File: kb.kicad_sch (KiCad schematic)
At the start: 182 parts, among them J1 Conn_01x04_Female, J2 10029449-001RLF, SW1 RotaryEncoder_Switch, U1 Pico, U2 SN74AHCT125D

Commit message: fixing sk6812s
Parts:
- D101, D102, D103, D104, D105, D106, D107, D108, D109, D110, D111, D112, D113, D114, D115, D116, D117, D118, D119, D120, D121, D122, D123, D124, D125, D126, D127, D128, D129, D130, D131, D132, D133, D134, D135, D136, D137, D138, D139, D140, D141, D142, D143, D144: symbol LED:SK6812MINI -> LED:WS2812B
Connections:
- net +5V: now also D101.1 (VDD), D102.1 (VDD), D103.1 (VDD), D104.1 (VDD), D105.1 (VDD), D106.1 (VDD), D107.1 (VDD), D108.1 (VDD), D109.1 (VDD), D110.1 (VDD), D111.1 (VDD), D112.1 (VDD), D113.1 (VDD), D114.1 (VDD), D115.1 (VDD), D116.1 (VDD), D117.1 (VDD), D118.1 (VDD), D119.1 (VDD), D120.1 (VDD), D121.1 (VDD), D122.1 (VDD), D123.1 (VDD), D124.1 (VDD), D125.1 (VDD), D126.1 (VDD), D127.1 (VDD), D128.1 (VDD), D129.1 (VDD), D130.1 (VDD), D131.1 (VDD), D132.1 (VDD), D133.1 (VDD), D134.1 (VDD), D135.1 (VDD), D136.1 (VDD), D137.1 (VDD), D138.1 (VDD), D139.1 (VDD), D140.1 (VDD), D141.1 (VDD), D142.1 (VDD), D143.1 (VDD), D144.1 (VDD); no longer D101.4 (VDD), D102.4 (VDD), D103.4 (VDD), D104.4 (VDD), D105.4 (VDD), D106.4 (VDD), D107.4 (VDD), D108.4 (VDD), D109.4 (VDD), D110.4 (VDD), D111.4 (VDD), D112.4 (VDD), D113.4 (VDD), D114.4 (VDD), D115.4 (VDD), D116.4 (VDD), D117.4 (VDD), D118.4 (VDD), D119.4 (VDD), D120.4 (VDD), D121.4 (VDD), D122.4 (VDD), D123.4 (VDD), D124.4 (VDD), D125.4 (VDD), D126.4 (VDD), D127.4 (VDD), D128.4 (VDD), D129.4 (VDD), D130.4 (VDD), D131.4 (VDD), D132.4 (VDD), D133.4 (VDD), D134.4 (VDD), D135.4 (VDD), D136.4 (VDD), D137.4 (VDD), D138.4 (VDD), D139.4 (VDD), D140.4 (VDD), D141.4 (VDD), D142.4 (VDD), D143.4 (VDD), D144.4 (VDD)
- net COL0: now also J2.6
- net COL1: now also J2.7
- net COL2: now also J2.8
- net COL3: now also J2.9
- net COL4: now also J2.10
- net COL5: now also J2.11
- net COL6: now also J2.12
- net COL7: now also J2.13
- net COL8: now also J2.14
- net ENC_R1: now also J2.16, U1.10 (GPIO7); no longer J2.15, U1.11 (GPIO8)
- net ENC_R2: now also J2.15, U1.11 (GPIO8); no longer J2.16, U1.10 (GPIO7)
- net GND: now also D101.3 (VSS), D102.3 (VSS), D103.3 (VSS), D104.3 (VSS), D105.3 (VSS), D106.3 (VSS), D107.3 (VSS), D108.3 (VSS), D109.3 (VSS), D110.3 (VSS), D111.3 (VSS), D112.3 (VSS), D113.3 (VSS), D114.3 (VSS), D115.3 (VSS), D116.3 (VSS), D117.3 (VSS), D118.3 (VSS), D119.3 (VSS), D120.3 (VSS), D121.3 (VSS), D122.3 (VSS), D123.3 (VSS), D124.3 (VSS), D125.3 (VSS), D126.3 (VSS), D127.3 (VSS), D128.3 (VSS), D129.3 (VSS), D130.3 (VSS), D131.3 (VSS), D132.3 (VSS), D133.3 (VSS), D134.3 (VSS), D135.3 (VSS), D136.3 (VSS), D137.3 (VSS), D138.3 (VSS), D139.3 (VSS), D140.3 (VSS), D141.3 (VSS), D142.3 (VSS), D143.3 (VSS), D144.3 (VSS); no longer D101.2 (VSS), D102.2 (VSS), D103.2 (VSS), D104.2 (VSS), D105.2 (VSS), D106.2 (VSS), D107.2 (VSS), D108.2 (VSS), D109.2 (VSS), D110.2 (VSS), D111.2 (VSS), D112.2 (VSS), D113.2 (VSS), D114.2 (VSS), D115.2 (VSS), D116.2 (VSS), D117.2 (VSS), D118.2 (VSS), D119.2 (VSS), D120.2 (VSS), D121.2 (VSS), D122.2 (VSS), D123.2 (VSS), D124.2 (VSS), D125.2 (VSS), D126.2 (VSS), D127.2 (VSS), D128.2 (VSS), D129.2 (VSS), D130.2 (VSS), D131.2 (VSS), D132.2 (VSS), D133.2 (VSS), D134.2 (VSS), D135.2 (VSS), D136.2 (VSS), D137.2 (VSS), D138.2 (VSS), D139.2 (VSS), D140.2 (VSS), D141.2 (VSS), D142.2 (VSS), D143.2 (VSS), D144.2 (VSS)
- net RGB_5V: now also D101.4 (DIN); no longer D101.3 (DIN)
- net RGB_TO_RIGHT: now also D143.2 (DOUT); no longer D143.1 (DOUT)
- net ROW9: now reaches J2.1
- net ROW9: now also U1.21 (GPIO16)
- net ROW8: now reaches J2.2
- net ROW8: now also U1.22 (GPIO17)
- net ROW7: now reaches J2.3
- net ROW7: now also U1.24 (GPIO18)
- net ROW6: now reaches J2.4
- net ROW6: now also U1.25 (GPIO19)
- net ROW5: now reaches J2.5
- net ROW5: now also U1.26 (GPIO20)
- new net: D102.2 (DOUT), D103.4 (DIN)
- new net: D101.2 (DOUT), D102.4 (DIN)
- new net: D106.2 (DOUT), D107.4 (DIN)
- new net: D105.2 (DOUT), D106.4 (DIN)
- new net: D107.2 (DOUT), D108.4 (DIN)
- new net: D138.2 (DOUT), D139.4 (DIN)
- new net: D137.2 (DOUT), D138.4 (DIN)
- new net: D109.4 (DIN), D144.2 (DOUT)
- new net: D108.2 (DOUT), D144.4 (DIN)
- new net: D135.2 (DOUT), D136.4 (DIN)
- new net: D134.2 (DOUT), D135.4 (DIN)
- new net: D104.2 (DOUT), D105.4 (DIN)
- new net: D103.2 (DOUT), D104.4 (DIN)
- new net: D115.2 (DOUT), D116.4 (DIN)
- new net: D114.2 (DOUT), D115.4 (DIN)
- new net: D112.2 (DOUT), D113.4 (DIN)
- new net: D111.2 (DOUT), D112.4 (DIN)
- new net: D128.2 (DOUT), D129.4 (DIN)
- new net: D127.2 (DOUT), D128.4 (DIN)
- new net: D124.2 (DOUT), D125.4 (DIN)
- new net: D123.2 (DOUT), D124.4 (DIN)
- new net: D129.2 (DOUT), D130.4 (DIN)
- new net: D122.2 (DOUT), D123.4 (DIN)
- new net: D139.2 (DOUT), D140.4 (DIN)
- new net: D136.2 (DOUT), D137.4 (DIN)
- new net: D140.2 (DOUT), D141.4 (DIN)
- new net: D121.2 (DOUT), D122.4 (DIN)
- new net: D120.2 (DOUT), D121.4 (DIN)
- new net: D130.2 (DOUT), D131.4 (DIN)
- new net: D116.2 (DOUT), D117.4 (DIN)
- new net: D126.2 (DOUT), D127.4 (DIN)
- new net: D125.2 (DOUT), D126.4 (DIN)
- new net: D142.2 (DOUT), D143.4 (DIN)
- new net: D141.2 (DOUT), D142.4 (DIN)
- new net: D110.2 (DOUT), D111.4 (DIN)
- new net: D109.2 (DOUT), D110.4 (DIN)
- new net: D119.2 (DOUT), D120.4 (DIN)
- new net: D118.2 (DOUT), D119.4 (DIN)
- new net: D133.2 (DOUT), D134.4 (DIN)
- new net: D132.2 (DOUT), D133.4 (DIN)
- new net: D113.2 (DOUT), D114.4 (DIN)
- new net: D131.2 (DOUT), D132.4 (DIN)
- new net: D117.2 (DOUT), D118.4 (DIN)

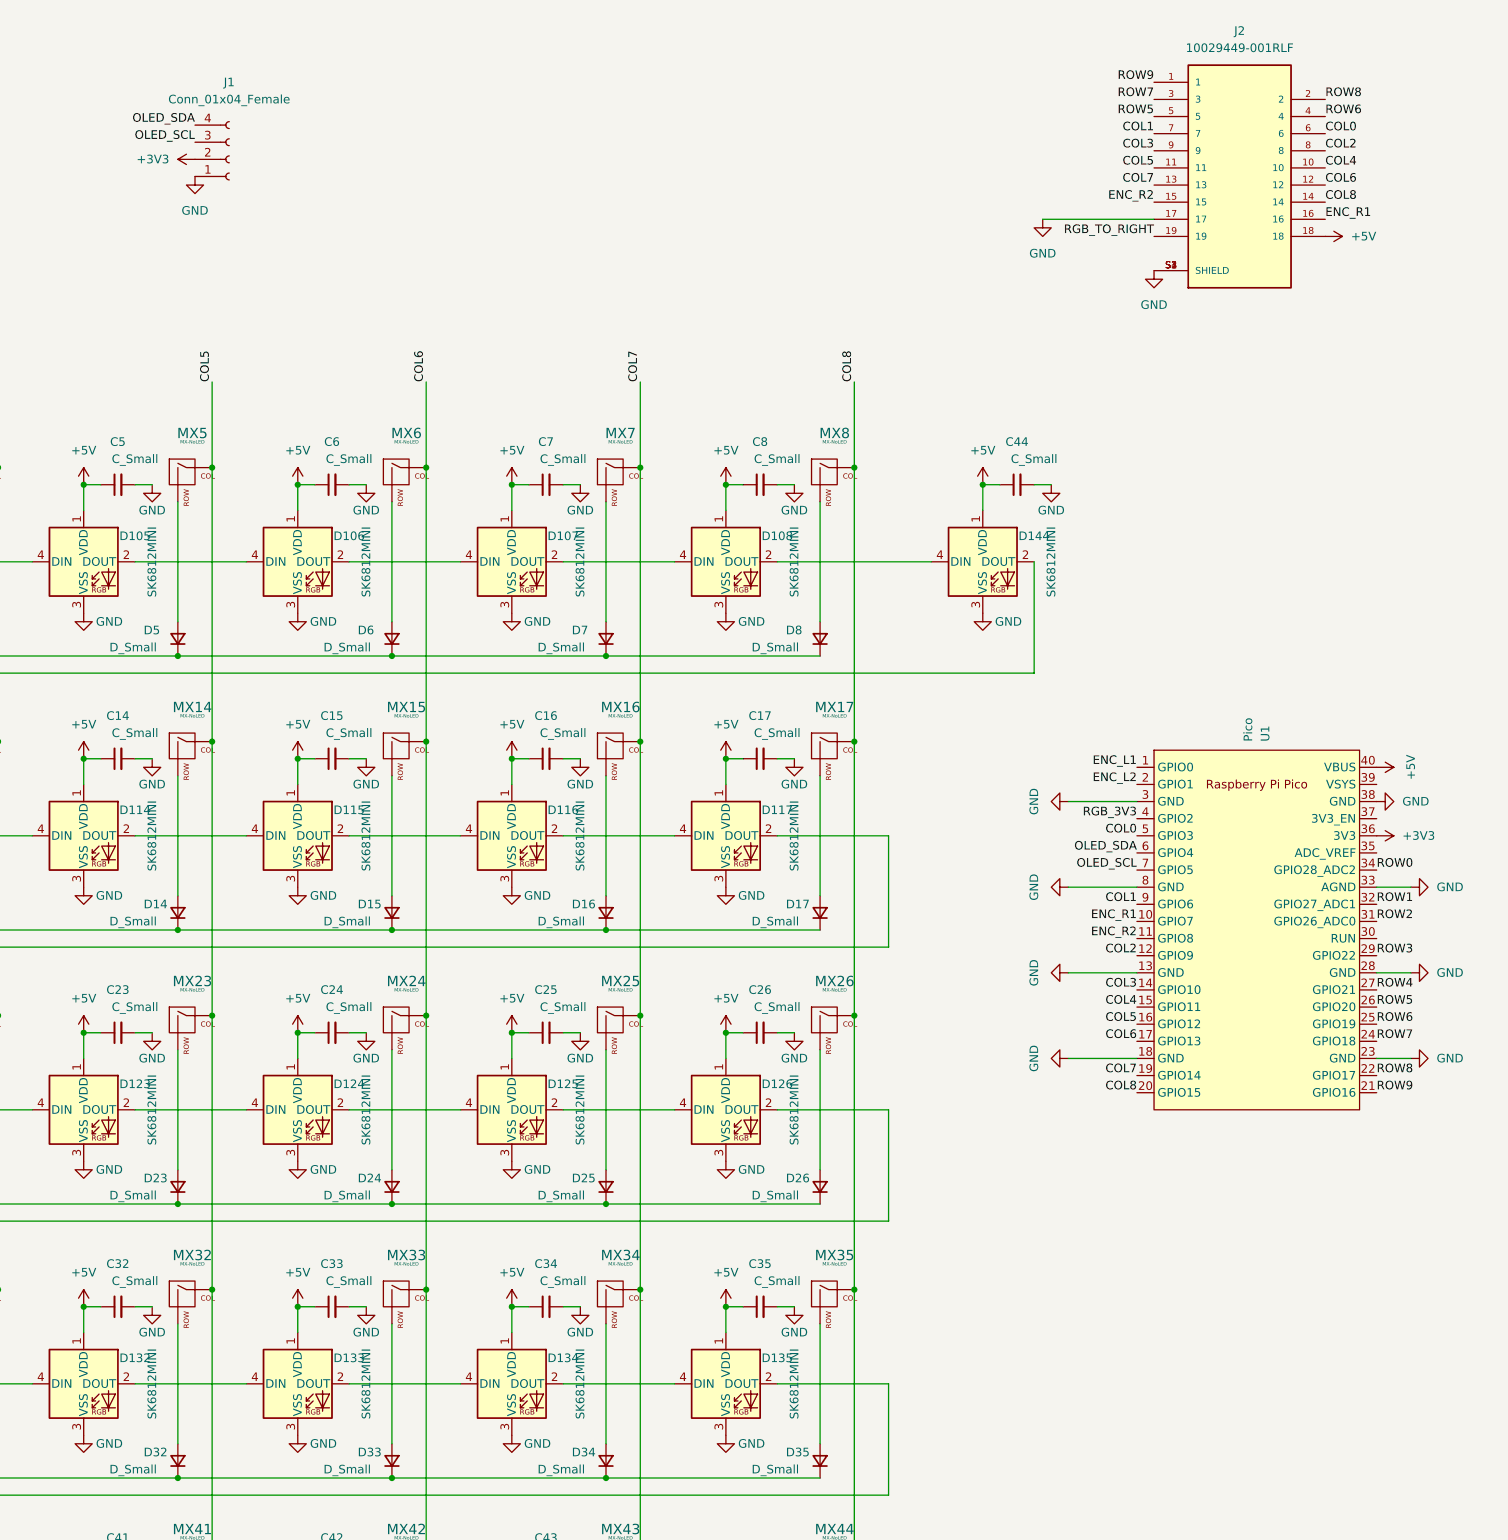
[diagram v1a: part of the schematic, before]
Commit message: start adding test points
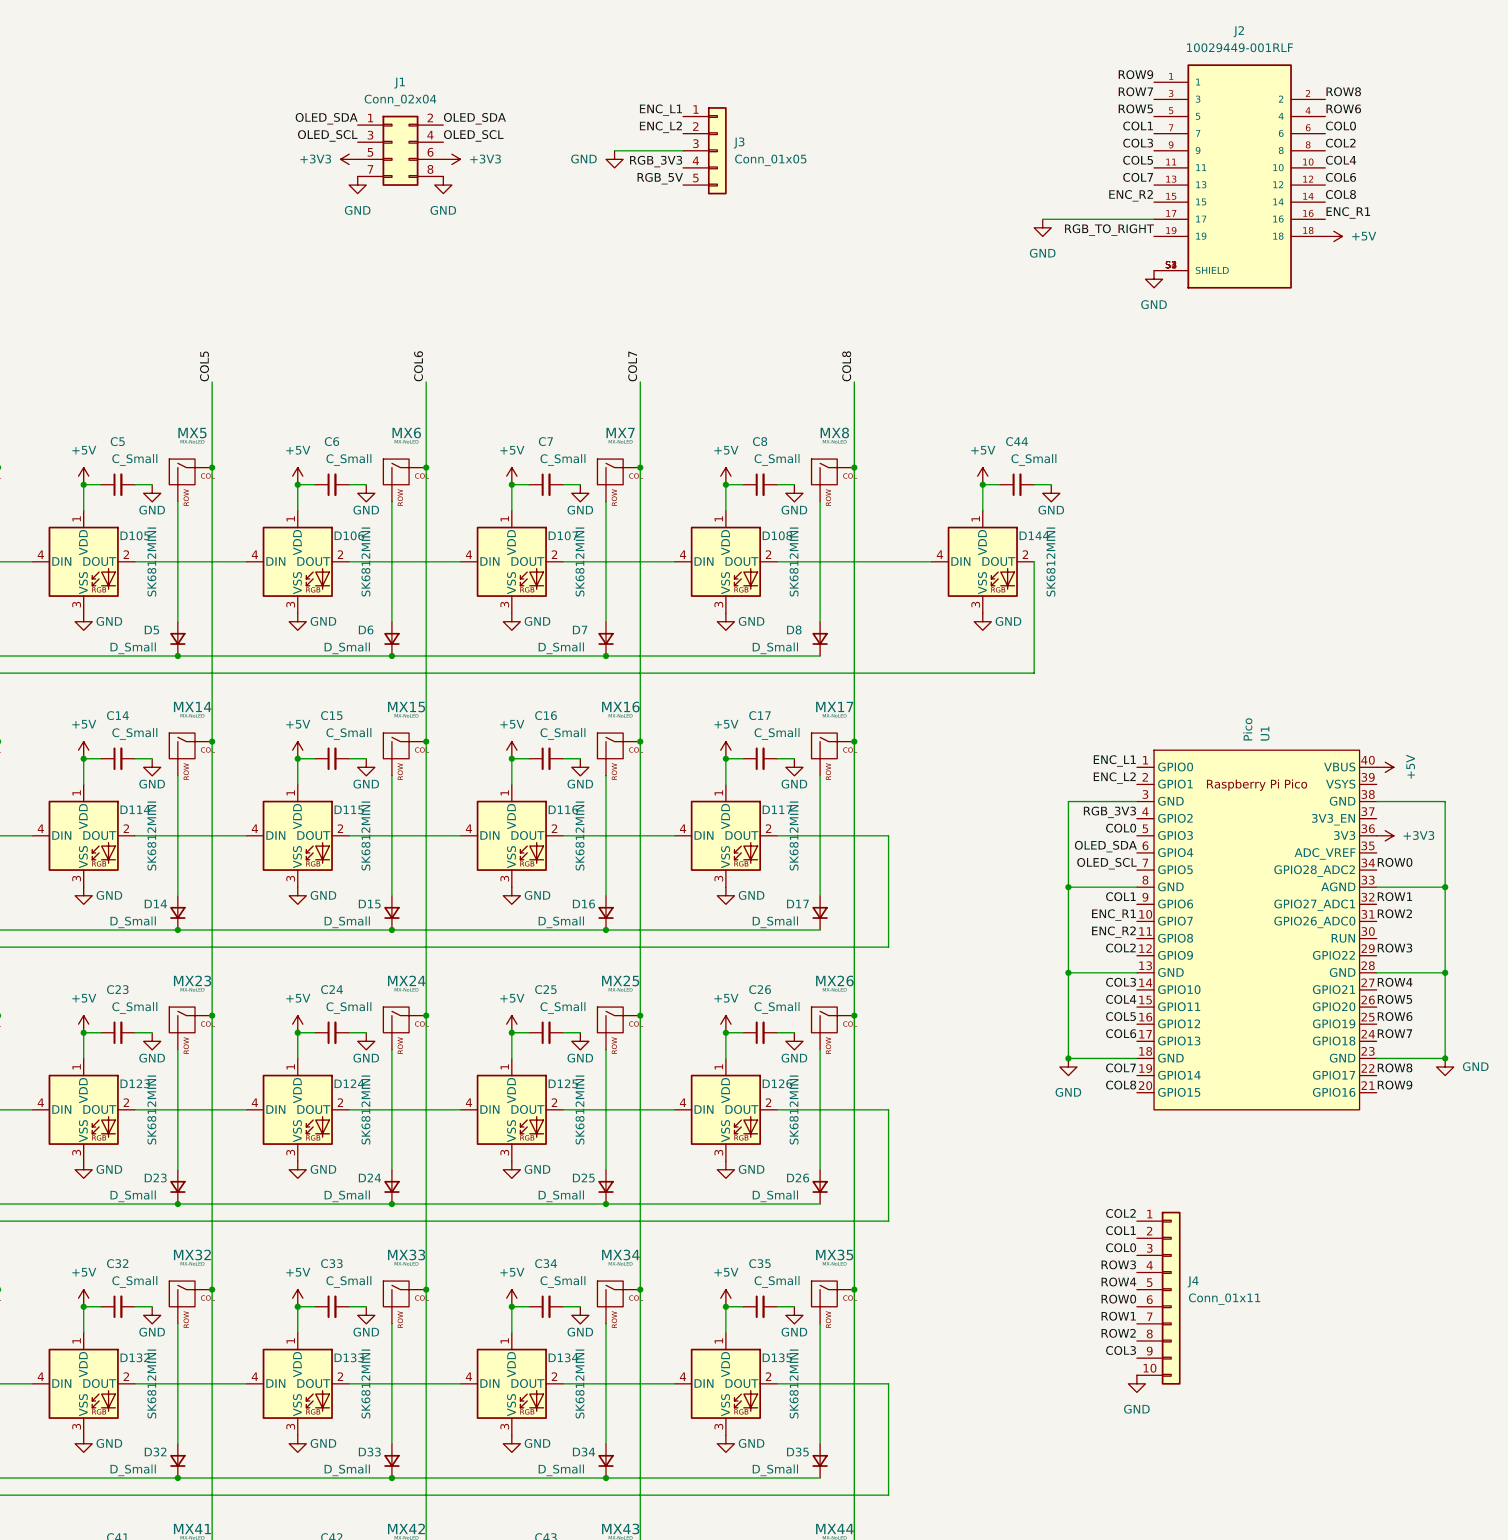
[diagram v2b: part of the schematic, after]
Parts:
- removed J1: Conn_01x04_Female, Connector_PinSocket_2.54mm:PinSocket_1x04_P2.54mm_Vertical, symbol Connector:Conn_01x04_Female
- added J1: Conn_02x04, Connector_PinHeader_2.54mm:PinHeader_2x04_P2.54mm_Vertical, symbol Connector_Generic:Conn_02x04_Odd_Even
- added J3: Conn_01x05, Connector_PinHeader_2.54mm:PinHeader_1x05_P2.54mm_Vertical, symbol Connector_Generic:Conn_01x05
- added J4: Conn_01x11, Connector_PinHeader_2.54mm:PinHeader_1x10_P2.54mm_Vertical, symbol Connector_Generic:Conn_01x10
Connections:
- net +3V3: now also J1.5 (Pin_5), J1.6 (Pin_6)
- net COL0: now also J4.3 (Pin_3)
- net COL1: now also J4.2 (Pin_2)
- net COL2: now also J4.1 (Pin_1)
- net COL3: now also J4.9 (Pin_9)
- net ENC_L1: now also J3.1 (Pin_1)
- net ENC_L2: now also J3.2 (Pin_2)
- net GND: now also J1.7 (Pin_7), J1.8 (Pin_8), J3.3 (Pin_3), J4.10 (Pin_10)
- net OLED_SCL: now also J1.3 (Pin_3), J1.4 (Pin_4)
- net OLED_SDA: now also J1.1 (Pin_1), J1.2 (Pin_2)
- net RGB_3V3: now also J3.4 (Pin_4)
- net RGB_5V: now also J3.5 (Pin_5)
- net ROW0: now also J4.6 (Pin_6)
- net ROW1: now also J4.7 (Pin_7)
- net ROW2: now also J4.8 (Pin_8)
- net ROW3: now also J4.4 (Pin_4)
- net ROW4: now also J4.5 (Pin_5)

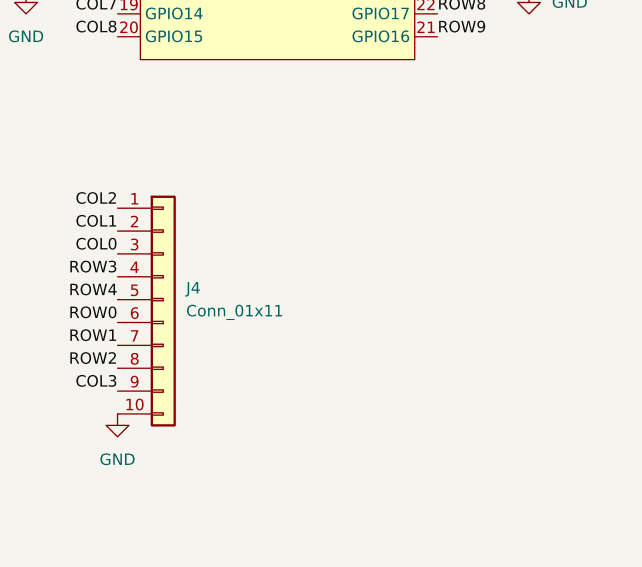
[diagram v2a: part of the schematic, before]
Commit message: Added test points
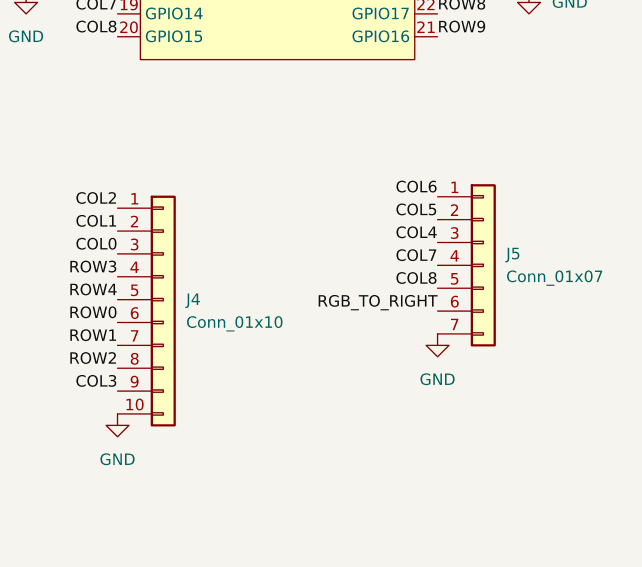
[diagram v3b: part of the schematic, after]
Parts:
- added J5: Conn_01x07, Connector_PinHeader_2.54mm:PinHeader_1x07_P2.54mm_Vertical, symbol Connector_Generic:Conn_01x07
- J4: value Conn_01x11 -> Conn_01x10
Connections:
- net COL4: now also J5.3 (Pin_3)
- net COL5: now also J5.2 (Pin_2)
- net COL6: now also J5.1 (Pin_1)
- net COL7: now also J5.4 (Pin_4)
- net COL8: now also J5.5 (Pin_5)
- net GND: now also J5.7 (Pin_7)
- net RGB_TO_RIGHT: now also J5.6 (Pin_6)
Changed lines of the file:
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@@
     (effects (font (size 1.27 1.27)) (justify right bottom))
   )
+  (label "COL4" (at 388.62 195.58 180)
+    (effects (font (size 1.27 1.27)) (justify right bottom))
+  )
   (label "ENC_L2" (at 285.75 30.48 180)
     (effects (font (size 1.27 1.27)) (justify right bottom))
@@
     (effects (font (size 1.27 1.27)) (justify left bottom))
   )
+  (label "COL8" (at 388.62 200.66 180)
+    (effects (font (size 1.27 1.27)) (justify right bottom))
+  )
   (label "ROW9" (at 355.6 22.86 180)
     (effects (font (size 1.27 1.27)) (justify right bottom))
@@
     (effects (font (size 1.27 1.27)) (justify left bottom))
   )
+  (label "RGB_TO_RIGHT" (at 388.62 203.2 180)
+    (effects (font (size 1.27 1.27)) (justify right bottom))
+  )
   (label "COL3" (at 353.06 212.09 180)
     (effects (font (size 1.27 1.27)) (justify right bottom))
@@
     (effects (font (size 1.27 1.27)) (justify left bottom))
   )
+  (label "COL6" (at 388.62 190.5 180)
+    (effects (font (size 1.27 1.27)) (justify right bottom))
+  )
   (label "ENC_L1" (at 353.06 124.46 180)
     (effects (font (size 1.27 1.27)) (justify right bottom))
@@
     (effects (font (size 1.27 1.27)) (justify right bottom))
   )
+  (label "COL5" (at 388.62 193.04 180)
+    (effects (font (size 1.27 1.27)) (justify right bottom))
+  )
   (label "COL0" (at 353.06 196.85 180)
     (effects (font (size 1.27 1.27)) (justify right bottom))
@@
     (effects (font (size 1.27 1.27)) (justify left bottom))
   )
+  (label "COL7" (at 388.62 198.12 180)
+    (effects (font (size 1.27 1.27)) (justify right bottom))
+  )
   (label "COL3" (at 355.6 33.02 180)
     (effects (font (size 1.27 1.27)) (justify right bottom))
@@
   (symbol (lib_id "Connector_Generic:Conn_01x10") (at 358.14 201.93 0) (unit 1)
     (in_bom yes) (on_board yes) (fields_autoplaced)
-    (property "Reference" "J4" (id 0) (at 360.68 200.6599 0)
+    (property "Reference" "J4" (id 0) (at 360.68 201.9299 0)
       (effects (font (size 1.27 1.27)) (justify left))
     )
-    (property "Value" "Conn_01x11" (id 1) (at 360.68 203.1999 0)
+    (property "Value" "Conn_01x10" (id 1) (at 360.68 204.4699 0)
       (effects (font (size 1.27 1.27)) (justify left))
     )
@@
     (pin "1")
   )
+  (symbol (lib_id "Connector_Generic:Conn_01x07") (at 393.7 198.12 0) (unit 1)
+    (in_bom yes) (on_board yes) (fields_autoplaced)
+    (property "Reference" "J5" (id 0) (at 396.24 196.8499 0)
+      (effects (font (size 1.27 1.27)) (justify left))
+    )
+    (property "Value" "Conn_01x07" (id 1) (at 396.24 199.3899 0)
+      (effects (font (size 1.27 1.27)) (justify left))
+    )
+    (property "Footprint" "Connector_PinHeader_2.54mm:PinHeader_1x07_P2.54mm_Vertical" (id 2) (at 393.7 198.12 0)
+      (effects (font (size 1.27 1.27)) hide)
+    )
+    (property "Datasheet" "~" (id 3) (at 393.7 198.12 0)
+      (effects (font (size 1.27 1.27)) hide)
+    )
+    (pin "1")
+    (pin "2")
+    (pin "3")
+    (pin "4")
+    (pin "5")
+    (pin "6")
+    (pin "7")
+  )
   (symbol (lib_id "Device:C_Small") (at 297.18 163.83 90) (unit 1)
     (in_bom yes) (on_board yes)
@@
     (pin "4")
   )
+  (symbol (lib_id "power:GND") (at 388.62 205.74 0) (unit 1)
+    (in_bom yes) (on_board yes) (fields_autoplaced)
+    (property "Reference" "#PWR04" (id 0) (at 388.62 212.09 0)
+      (effects (font (size 1.27 1.27)) hide)
+    )
+    (property "Value" "GND" (id 1) (at 388.62 210.82 0))
+    (property "Footprint" "" (id 2) (at 388.62 205.74 0)
+      (effects (font (size 1.27 1.27)) hide)
+    )
+    (property "Datasheet" "" (id 3) (at 388.62 205.74 0)
+      (effects (font (size 1.27 1.27)) hide)
+    )
+    (pin "1")
+  )
   (symbol (lib_id "power:+5V") (at 292.1 82.55 0) (unit 1)
     (in_bom yes) (on_board yes) (fields_autoplaced)
@@
       (reference "#PWR03") (unit 1) (value "+5V") (footprint "")
     )
+    (path "/e1d5c413-66bd-47c2-8cc9-a5bc0c1cf3d6"
+      (reference "#PWR04") (unit 1) (value "GND") (footprint "")
+    )
     (path "/53f67357-c441-4e08-a422-cc01051c969e"
       (reference "#PWR07") (unit 1) (value "GND") (footprint "")
@@
     )
     (path "/30794163-d0ff-4fbd-a518-faf7b2580234"
-      (reference "J4") (unit 1) (value "Conn_01x11") (footprint "Connector_PinHeader_2.54mm:PinHeader_1x10_P2.54mm_Vertical")
+      (reference "J4") (unit 1) (value "Conn_01x10") (footprint "Connector_PinHeader_2.54mm:PinHeader_1x10_P2.54mm_Vertical")
+    )
+    (path "/4db1fb8f-f787-4a69-92ca-375518b2c034"
+      (reference "J5") (unit 1) (value "Conn_01x07") (footprint "Connector_PinHeader_2.54mm:PinHeader_1x07_P2.54mm_Vertical")
     )
     (path "/8a089bf5-08f1-41ee-aa36-391f5cdf0f9d"
